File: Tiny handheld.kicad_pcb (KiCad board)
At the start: 2 copper layers, 34.3 x 58.4 mm, 44 parts, among them IC1 BQ21040DBVR, J1 VDisplay/prog1, J2 HDisplay/prog, J3 USB_C_Receptacle_USB2.0, U1 ATtiny85-20P, U2 ATtiny85-20S

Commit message: wiring part 1
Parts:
- removed C1: 1uF 16V, Capacitor_SMD:C_1206_3216Metric_Pad1.33x1.80mm_HandSolder
- removed the REF** at (136.4, 75.2)
- moved R7 30.3 mm to (136.7, 109.2)
- moved R1 23.1 mm to (136.7, 112.8)
- moved JP3 22.4 mm to (159.0, 128.0)
- moved JP2 0.13 mm to (142.7, 128.0)
- turned R14 to 0 degrees
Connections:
- S2 pad 7: (no net) -> GND
- S2 pad 8: (no net) -> GND
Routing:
- net PB5/RES: track 0.00 -> 113.1 mm, vias 0 -> 5
- net PB2/SCL/SCK: track 0.00 -> 64.6 mm, vias 0 -> 5
- net PB0/SDA/MOSI: track 0.00 -> 63.6 mm, vias 0 -> 4
- net Net-(D1-Pad2): track 0.00 -> 61.1 mm, vias 0 -> 5
- net ExtVCC: track 0.00 -> 45.4 mm, vias 0 -> 4
- net PB1/MISO: track 0.00 -> 43.8 mm, vias 0 -> 4
- net Net-(D2-Pad1): track 0.00 -> 43.7 mm, vias 0 -> 2
- net VCC: track 0.00 -> 41.7 mm, vias 0 -> 3
- net PB3: track 0.00 -> 40.3 mm, vias 0 -> 2
- net Net-(JP1-Pad3): track 0.00 -> 39.9 mm, vias 0 -> 2
- net Net-(R3-Pad2): track 0.00 -> 33.5 mm, vias 0 -> 1
- net Net-(C2-Pad1): track 0.00 -> 32.4 mm, vias 0 -> 1
- net Net-(R5-Pad2): track 0.00 -> 26.8 mm, vias 0 -> 1
- net Net-(J3-PadA5): track 0.00 -> 26.1 mm, vias 0 -> 1
- net Net-(R4-Pad2): track 0.00 -> 14.3 mm, vias 0 -> 1
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
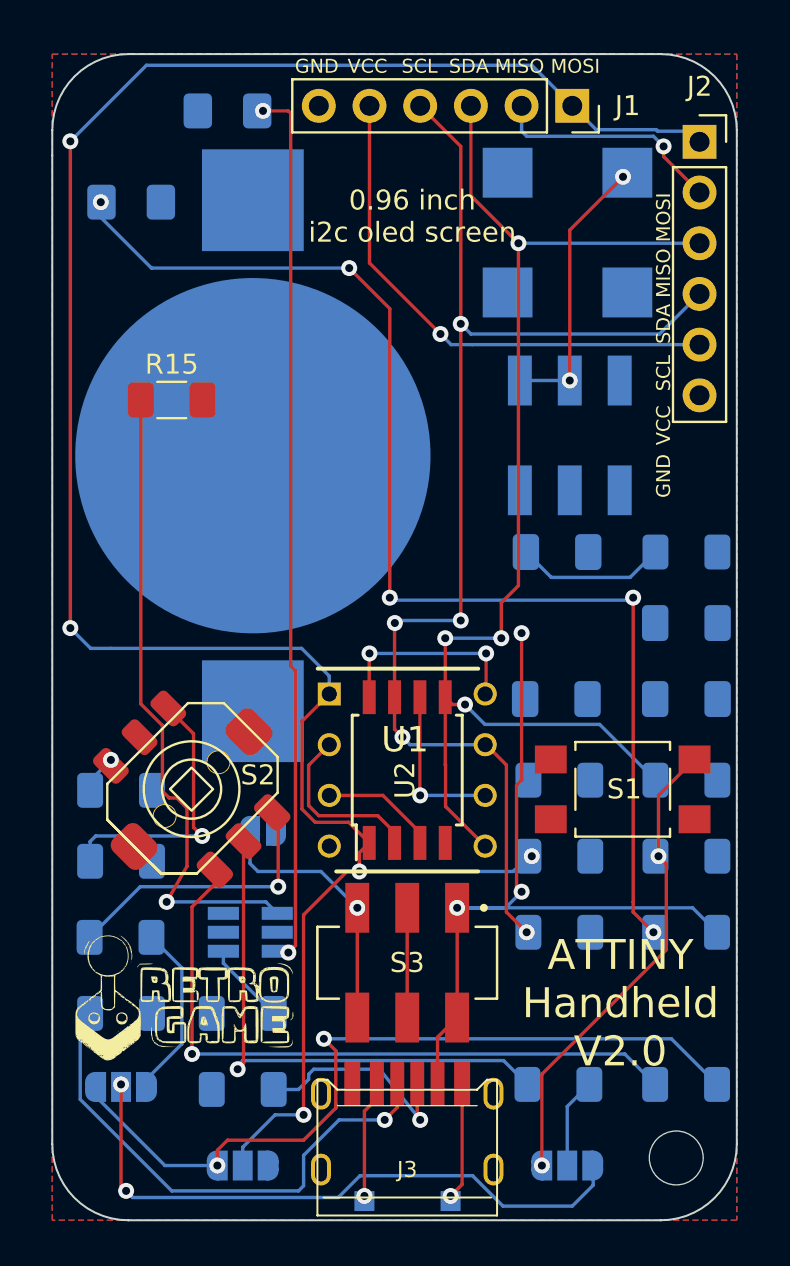
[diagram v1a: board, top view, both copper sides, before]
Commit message: completed routing, started erc
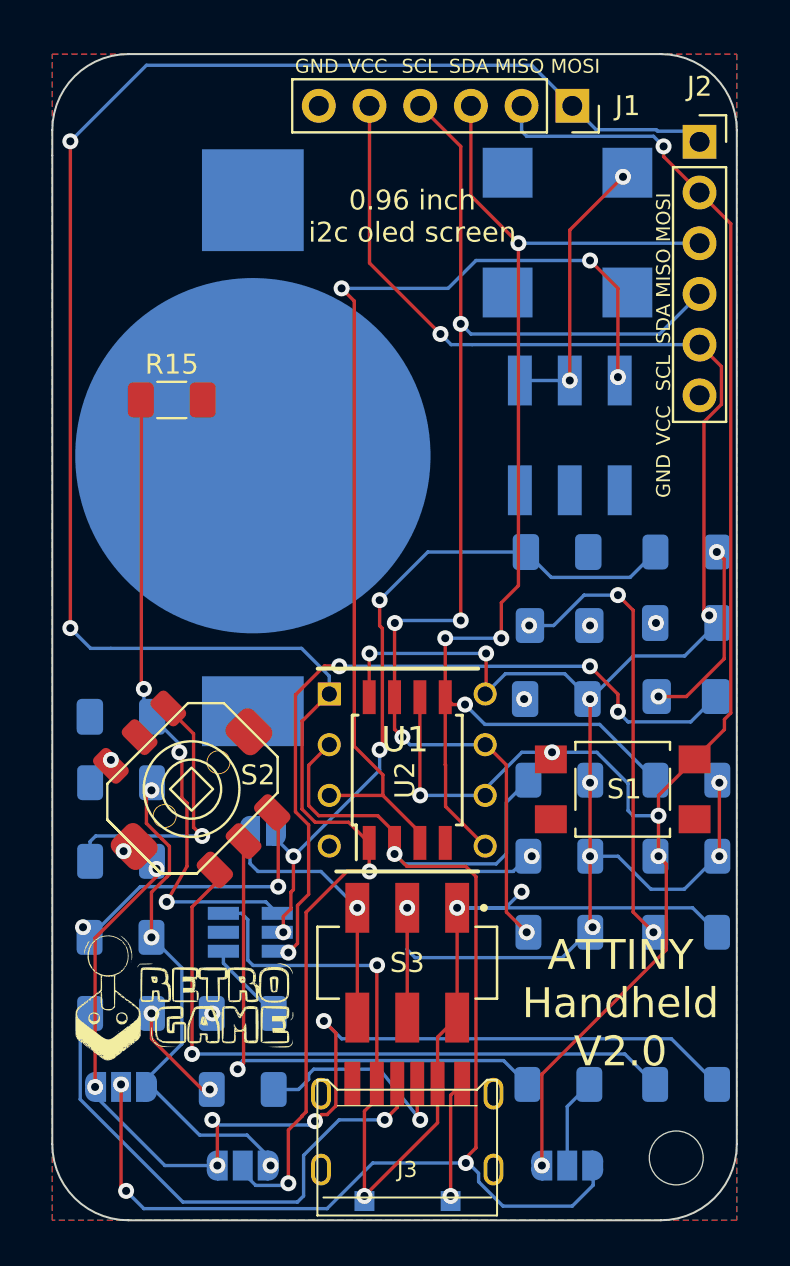
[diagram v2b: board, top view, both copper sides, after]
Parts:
- moved D2 37.3 mm to (165.0, 104.5)
- moved D1 30.2 mm to (158.6, 101.0)
- moved C2 28.3 mm to (136.7, 105.5)
- moved R7 0.38 mm to (136.7, 108.8)
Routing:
- net VCC: track 41.7 -> 105.4 mm, vias 3 -> 11
- net PB4: track 5.83 -> 51.5 mm, vias 0 -> 3
- net PB1/MISO: track 43.8 -> 85.4 mm, vias 4 -> 6
- net Net-(D1-Pad2): track 61.1 -> 22.7 mm, vias 5 -> 3
- net PB3: track 40.3 -> 71.4 mm, vias 2 -> 4
- net Net-(C6-Pad1): track 7.54 -> 36.3 mm, vias 0 -> 4
- net Net-(JP1-Pad1): track 8.85 -> 25.2 mm, vias 0 -> 3
- net Net-(JP1-Pad3): track 39.9 -> 55.0 mm, vias 2 -> 6
- net Net-(D2-Pad2): track 0.00 -> 9.57 mm, vias 0 -> 2
- net ExtVCC: track 45.4 -> 54.5 mm
- net Net-(D2-Pad1): track 43.7 -> 37.5 mm, vias 2 -> 4
- net GND: track 5.86 -> 11.1 mm, vias 1 -> 8
- net PB5/RES: track 113.1 -> 115.0 mm
- net Net-(J3-PadA5): track 26.1 -> 26.9 mm
- net Net-(R4-Pad2): track 14.3 -> 14.6 mm, vias 1 -> 2
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
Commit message: ERC finished (with some exclusions)
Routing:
- net ExtVCC: track 54.5 -> 50.9 mm, vias 4 -> 3
- net PB2/SCL/SCK: track 64.6 -> 63.9 mm
- net Net-(R4-Pad2): track 14.6 -> 14.3 mm, vias 2 -> 1
- net Net-(JP1-Pad1): vias 3 -> 2
- net PB5/RES: vias 5 -> 4
- net Net-(D1-Pad2): vias 3 -> 2
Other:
- board text removed: "C"

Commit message: V2.0 Finished
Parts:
- added REF**: OSHW-Logo2_7.3x6mm_SilkScreen, Symbol:OSHW-Logo2_7.3x6mm_SilkScreen, B.Cu at (151.0, 112.1)
- moved R15 5.04 mm to (134.7, 91.9), turned to 90 degrees
- moved G*** 0.46 mm to (139.6, 120.1)
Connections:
- S2 pad 7: GND -> (no net)
- S2 pad 8: GND -> (no net)
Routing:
- net Net-(C2-Pad1): track 32.2 -> 29.4 mm
- net Net-(D2-Pad1): track 37.5 -> 36.9 mm
- net GND: vias 8 -> 7
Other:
- board text added: "NTC"
- board text added: "PWR"
- board text added: "RST"
- board text added: "X"
- board text added: "sound"
- board text added: "←"
- board text removed: "-"
- board text removed: "MOSI"

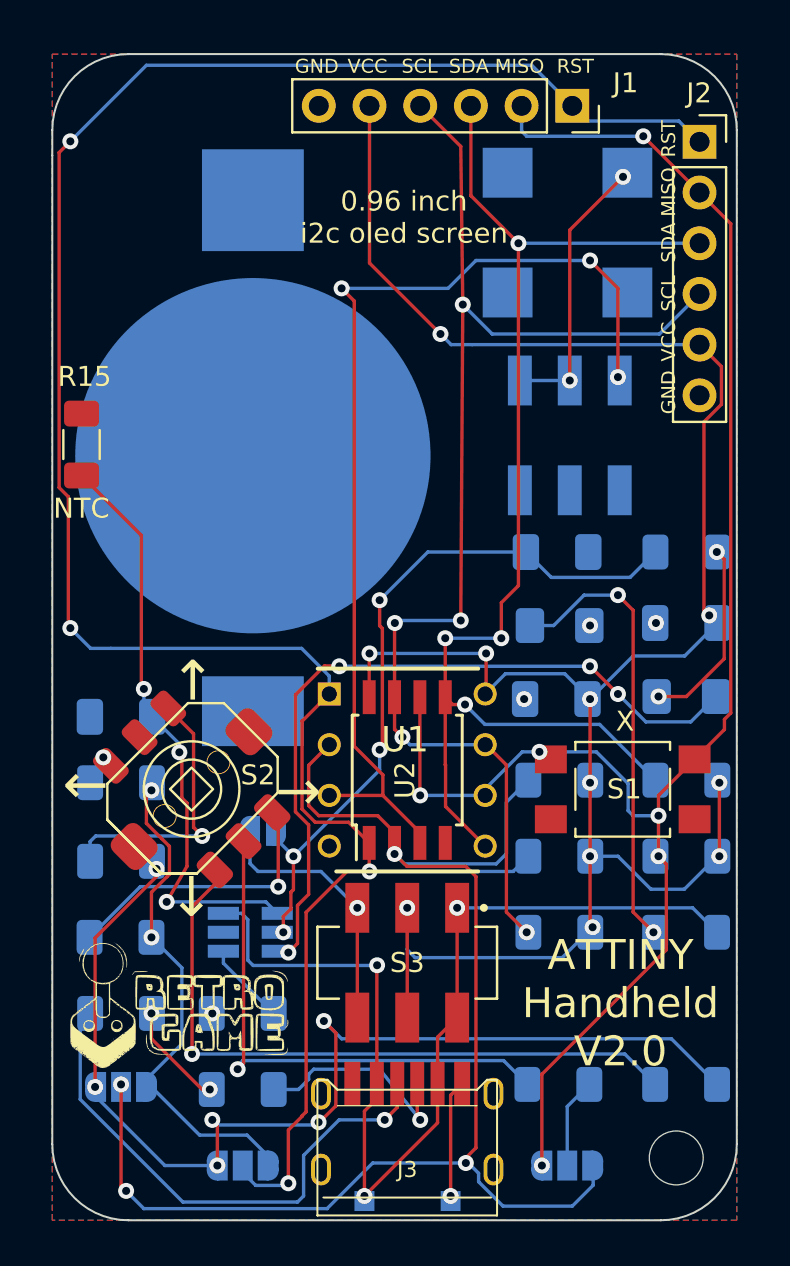
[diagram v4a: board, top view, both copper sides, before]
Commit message: fames rounded tracks added
added bom
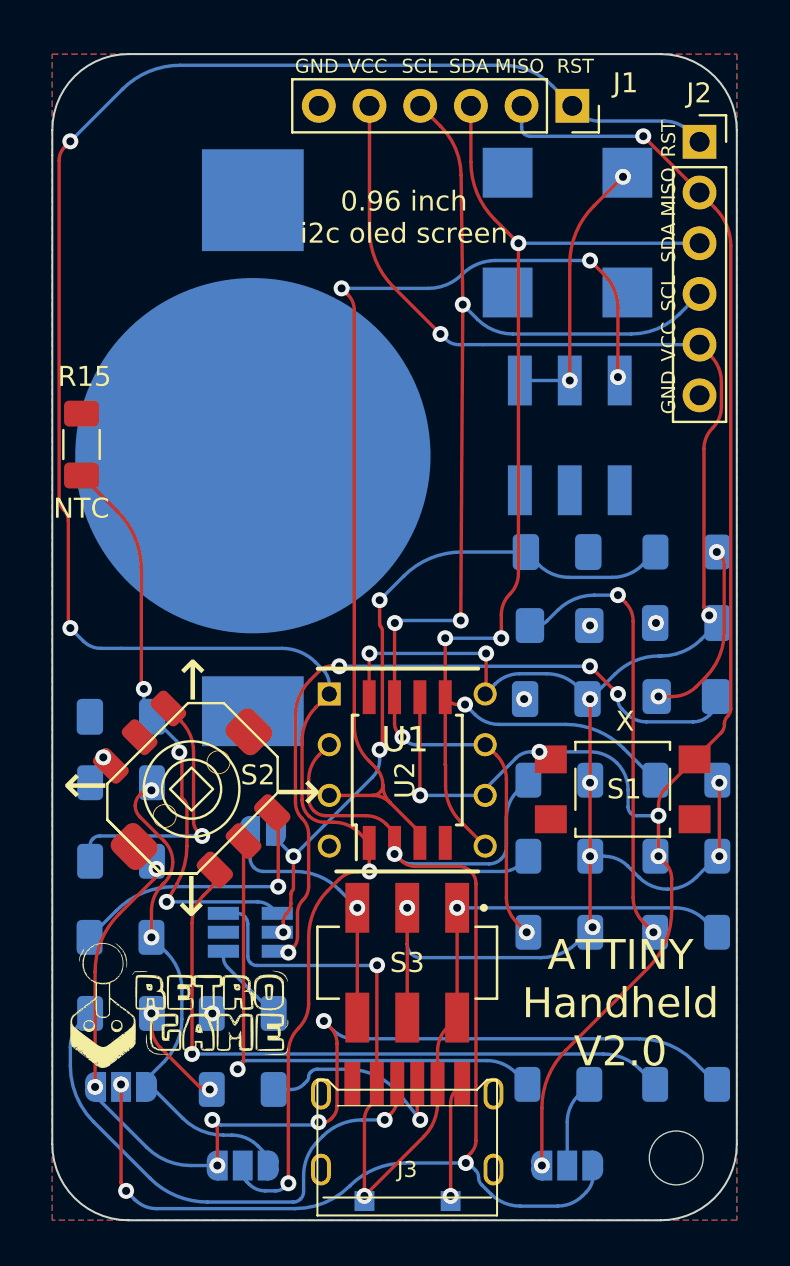
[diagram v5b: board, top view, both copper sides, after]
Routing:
- net VCC: track 105.4 -> 104.0 mm
- net PB3: track 71.4 -> 70.0 mm
- net PB5/RES: track 115.4 -> 114.1 mm
- net PB2/SCL/SCK: track 64.2 -> 63.3 mm
- net PB1/MISO: track 85.2 -> 84.5 mm
- net Net-(C6-Pad1): track 36.3 -> 35.6 mm
- net PB4: track 51.5 -> 52.1 mm
- net Net-(JP1-Pad3): track 54.8 -> 54.2 mm

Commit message: enh tracks
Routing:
- net PB5/RES: track 114.1 -> 115.8 mm
- net VCC: track 104.0 -> 105.4 mm
- net PB3: track 70.0 -> 71.4 mm
- net PB1/MISO: track 84.5 -> 85.7 mm
- net Net-(JP1-Pad1): track 25.0 -> 26.0 mm
- net PB2/SCL/SCK: track 63.3 -> 64.2 mm
- net Net-(JP1-Pad3): track 54.2 -> 55.1 mm
- net Net-(J3-PadA5): track 26.7 -> 27.5 mm
- net Net-(C6-Pad1): track 35.6 -> 36.3 mm
- net Net-(D2-Pad1): track 37.0 -> 37.6 mm
- net PB4: track 52.1 -> 51.5 mm

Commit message: cleanup
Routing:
- net GND: track 11.1 -> 22.9 mm, vias 7 -> 15
- net PB5/RES: track 115.8 -> 114.1 mm
- net VCC: track 105.4 -> 104.0 mm
- net PB3: track 71.4 -> 69.9 mm
- net PB1/MISO: track 85.7 -> 84.5 mm
- net Net-(JP1-Pad1): track 26.0 -> 25.0 mm
- net PB2/SCL/SCK: track 64.2 -> 63.3 mm
- net Net-(JP1-Pad3): track 55.1 -> 54.2 mm
- net Net-(J3-PadA5): track 27.5 -> 26.7 mm
- net Net-(C6-Pad1): track 36.3 -> 35.6 mm
- net Net-(D2-Pad1): track 37.6 -> 37.0 mm
- net PB4: track 51.5 -> 52.1 mm
